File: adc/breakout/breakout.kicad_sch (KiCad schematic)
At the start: 70 parts, among them J1 Conn_01x05_Pin, J2 Conn_01x05_Pin, J3 Conn_01x03_Pin, J4 Conn_01x06_Pin, U1 ESD5344D-TP, U2 ADS1261IRHBR, U3 ESD5344D-TP, U4 ESD5344D-TP, U5 TPS7A2050PDBVR, U6 TPS61252DSG, U7 XC6206P332MR

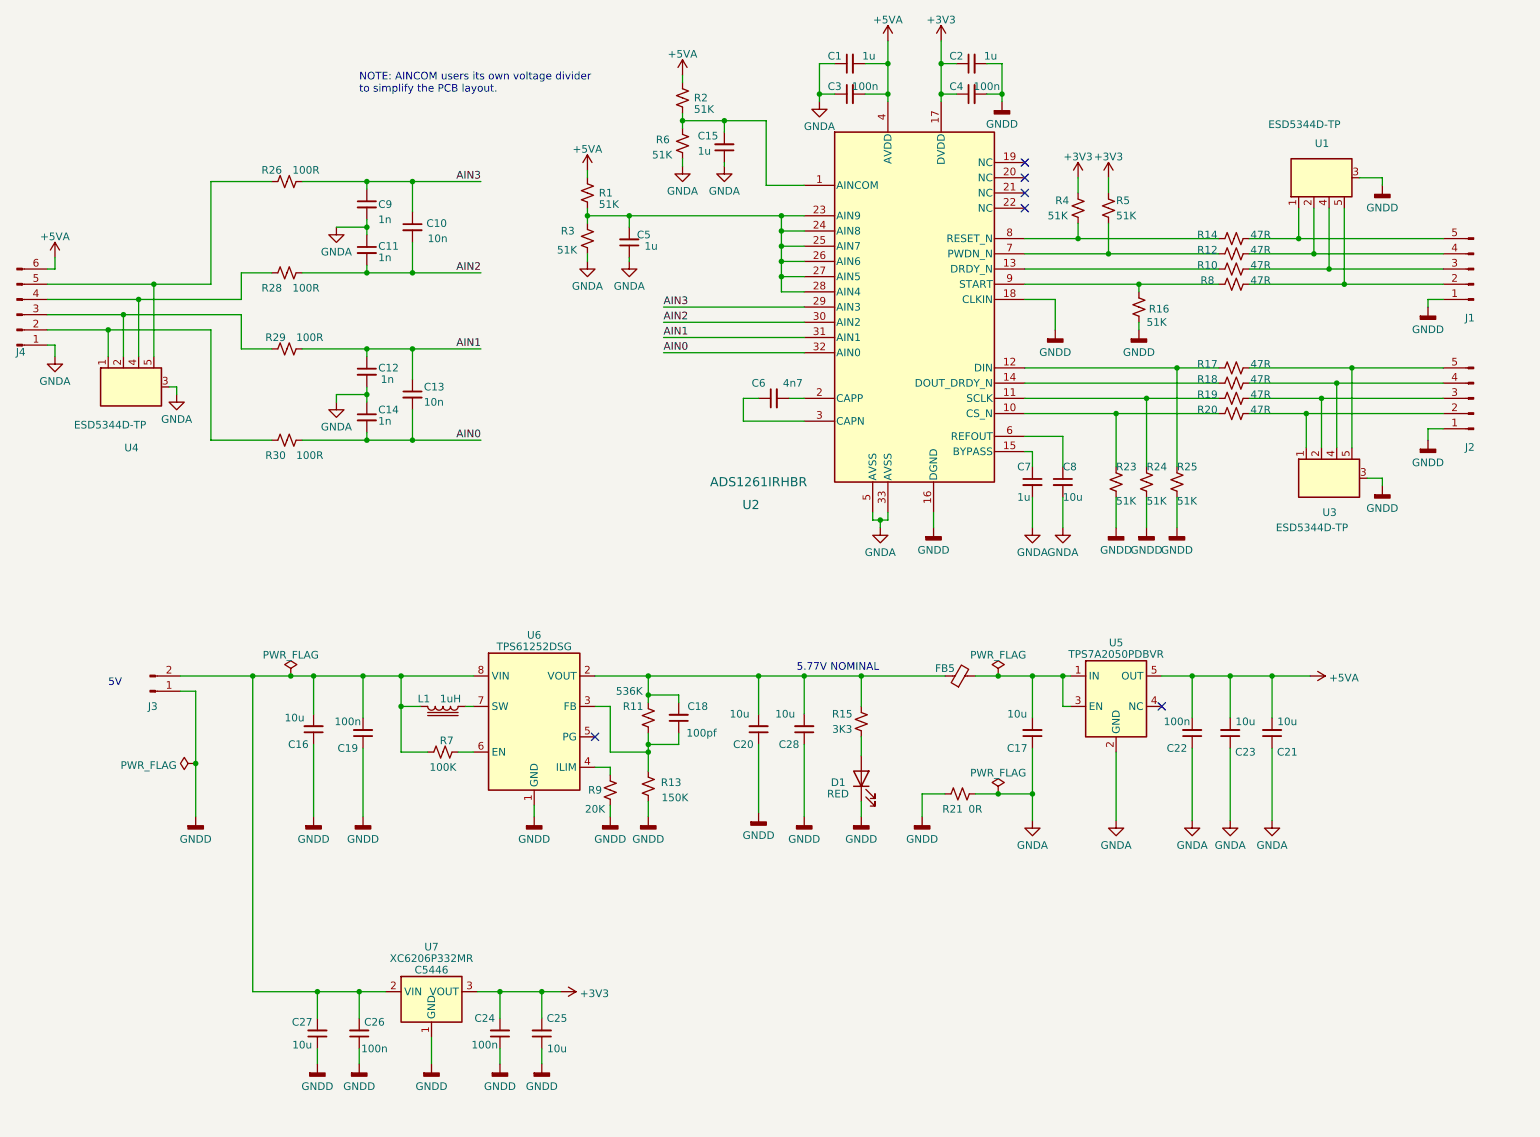
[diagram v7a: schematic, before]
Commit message: Minor schematic reformatting.
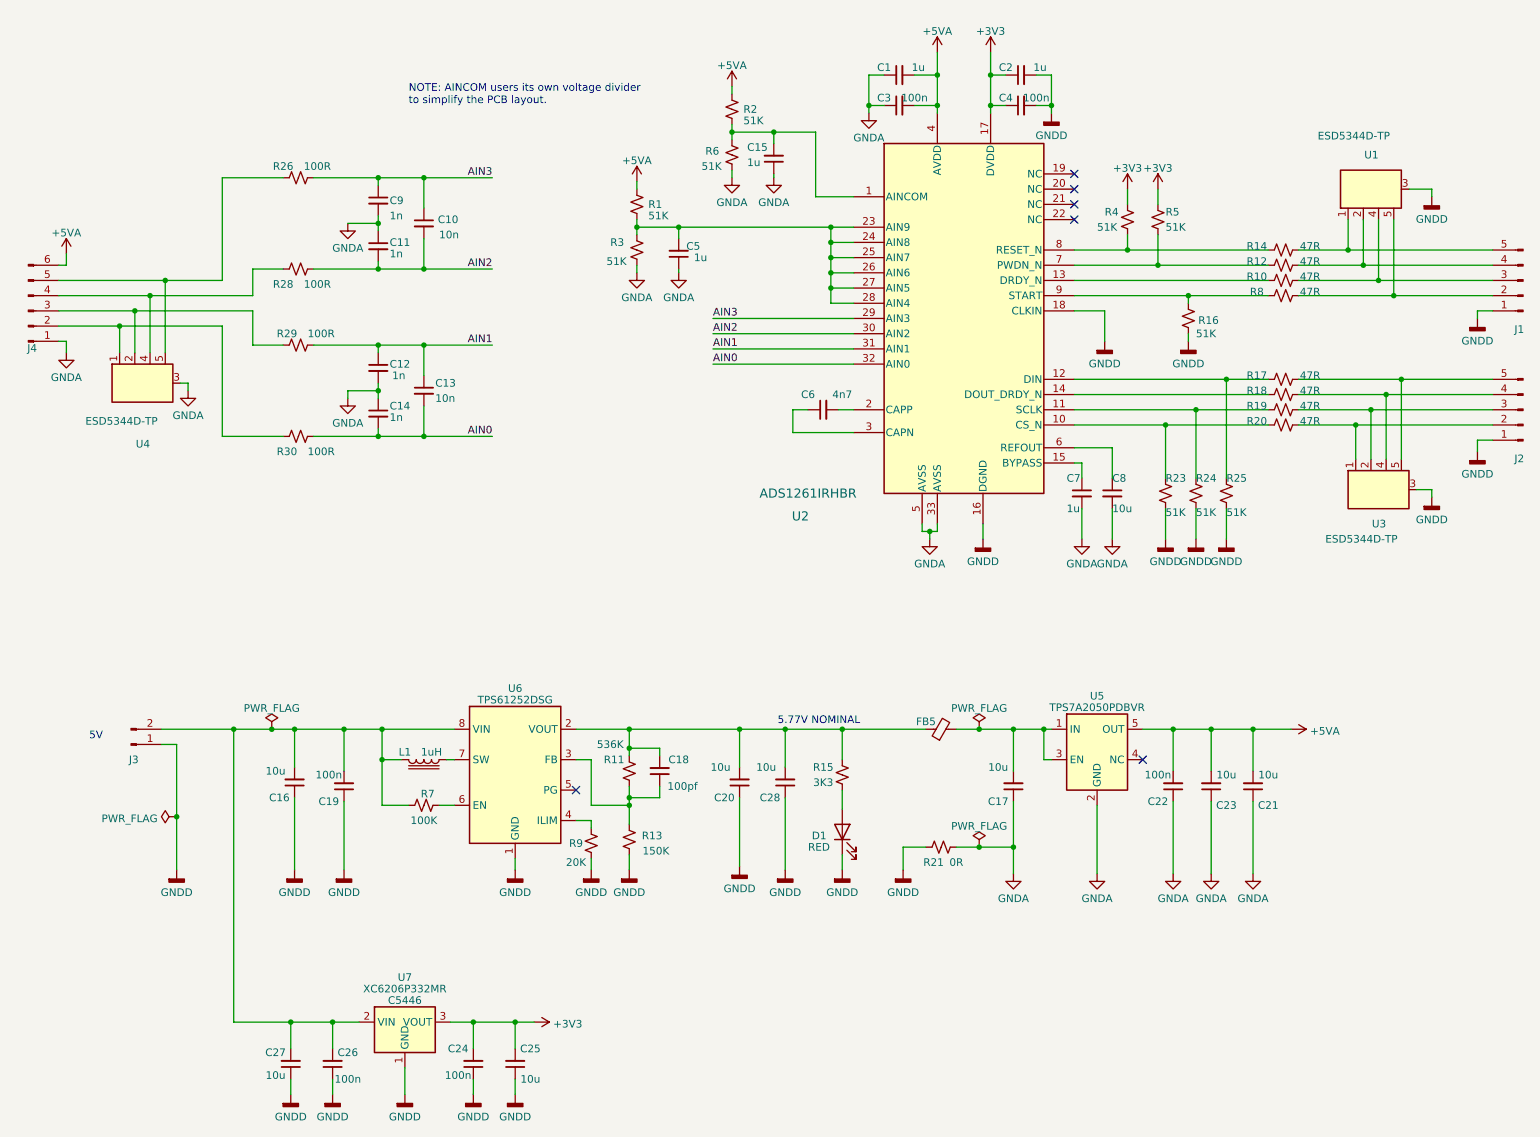
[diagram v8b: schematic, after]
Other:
- moved on the sheet: C1, C10, C11, C12, C13, C14, C15, C16, C17, C18, C19, C2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
